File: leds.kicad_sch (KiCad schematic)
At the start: 193 parts

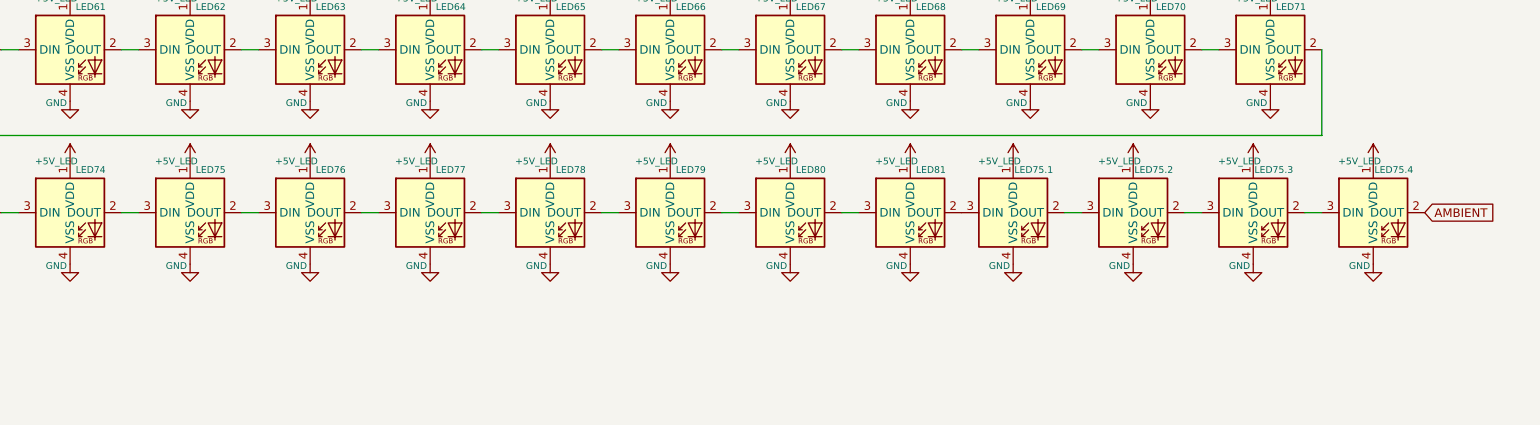
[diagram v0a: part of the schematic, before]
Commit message: Implemented multiple leds for spacebar
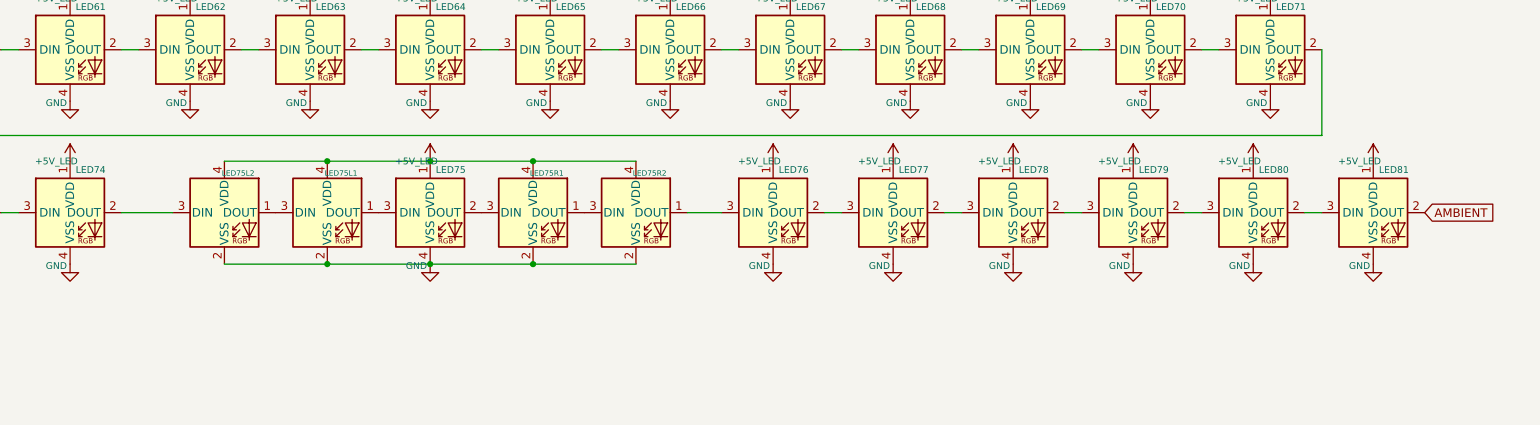
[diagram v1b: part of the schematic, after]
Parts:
- removed LED75.1, LED75.2, LED75.3, LED75.4: SK6812, PCM_marbastlib-various:LED_6028R, symbol PCM_marbastlib-various:SK6812MINI-E
- added LED75L1, LED75L2, LED75R1, LED75R2: WS2812_2020, PCM_marbastlib-various:LED_WS2812_2020, symbol PCM_marbastlib-various:WS2812_2020
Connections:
- net +5V_LED: now also LED75L1.4 (VDD), LED75L2.4 (VDD), LED75R1.4 (VDD), LED75R2.4 (VDD)
- net AMBIENT: now also LED81.2 (DOUT)
- net GND: now also LED75L1.2 (VSS), LED75L2.2 (VSS), LED75R1.2 (VSS), LED75R2.2 (VSS)
- net at LED74.2 (DOUT): now also LED75L2.3 (DIN); no longer LED75.3 (DIN)
- net at LED76.3 (DIN): now also LED75R2.1 (DOUT); no longer LED75.2 (DOUT)
- new net: LED75R1.1 (DOUT), LED75R2.3 (DIN)
- new net: LED75L1.3 (DIN), LED75L2.1 (DOUT)
- new net: LED75.2 (DOUT), LED75R1.3 (DIN)
- new net: LED75.3 (DIN), LED75L1.1 (DOUT)
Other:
- moved on the sheet: LED75, LED76, LED77, LED78, LED79, LED80, LED81

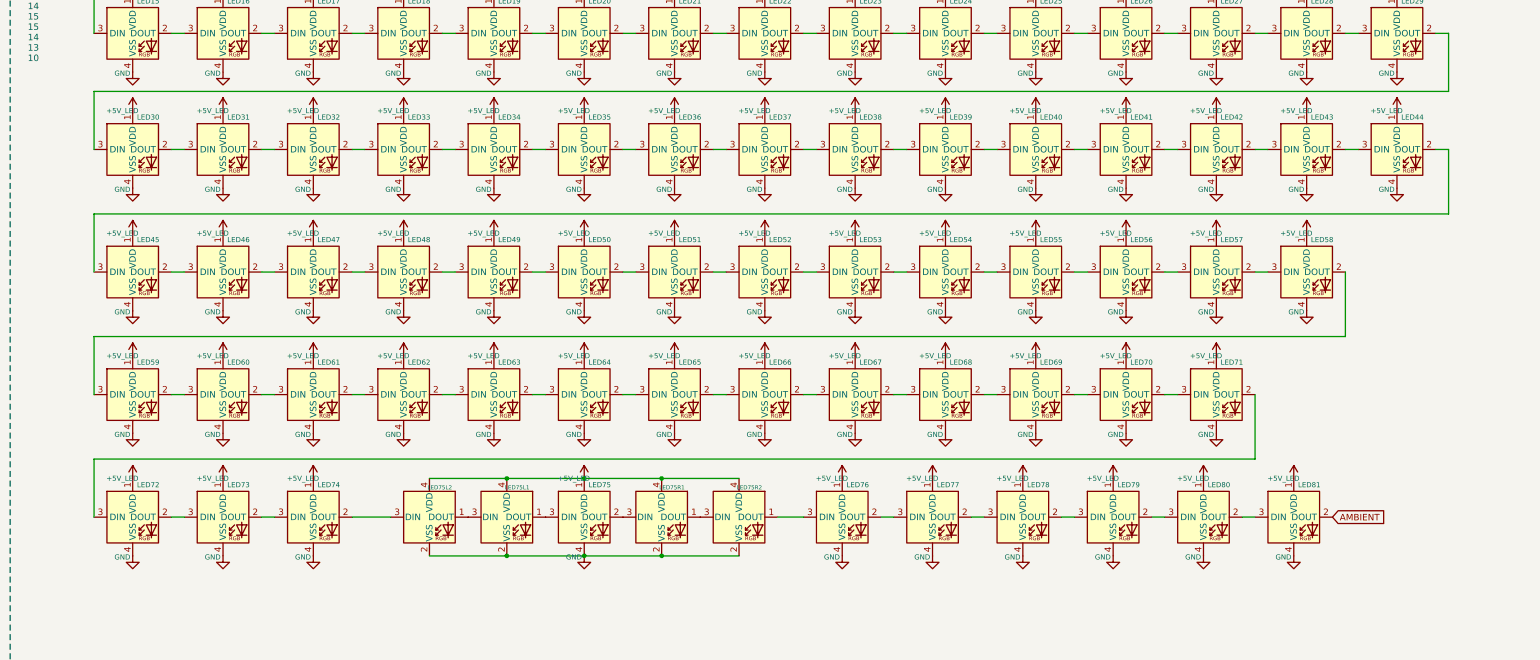
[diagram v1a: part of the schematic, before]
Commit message: Rev 2: Major PCB rework — haptic motor, MicroSD, NTC, CTP, split spacebar
- Added ERM haptic motor with BSS138 MOSFET driver on GP21
- Added MicroSD card slot (MSD-1-A, push-in/auto-eject)
- Added NTC thermistor with voltage divider
- Added 4-pin 0.5mm FPC connector for capacitive touch panel
- Added ferrite beads (0603 600R, 0805) for power filtering
- Added 1N4148WT protection diode and test point
- Split spacebar support: HE45 alternate 1.75u stabilizer footprint
- Full PCB re-route with 4-layer switch footprints
- All 81 hall sensors relabeled with key names in schematic
- Relaxed DRC (text height, via diameter), new via size 0.6/0.2
- Added CHANGELOG.md and wiring.cpp MUX mapping reference
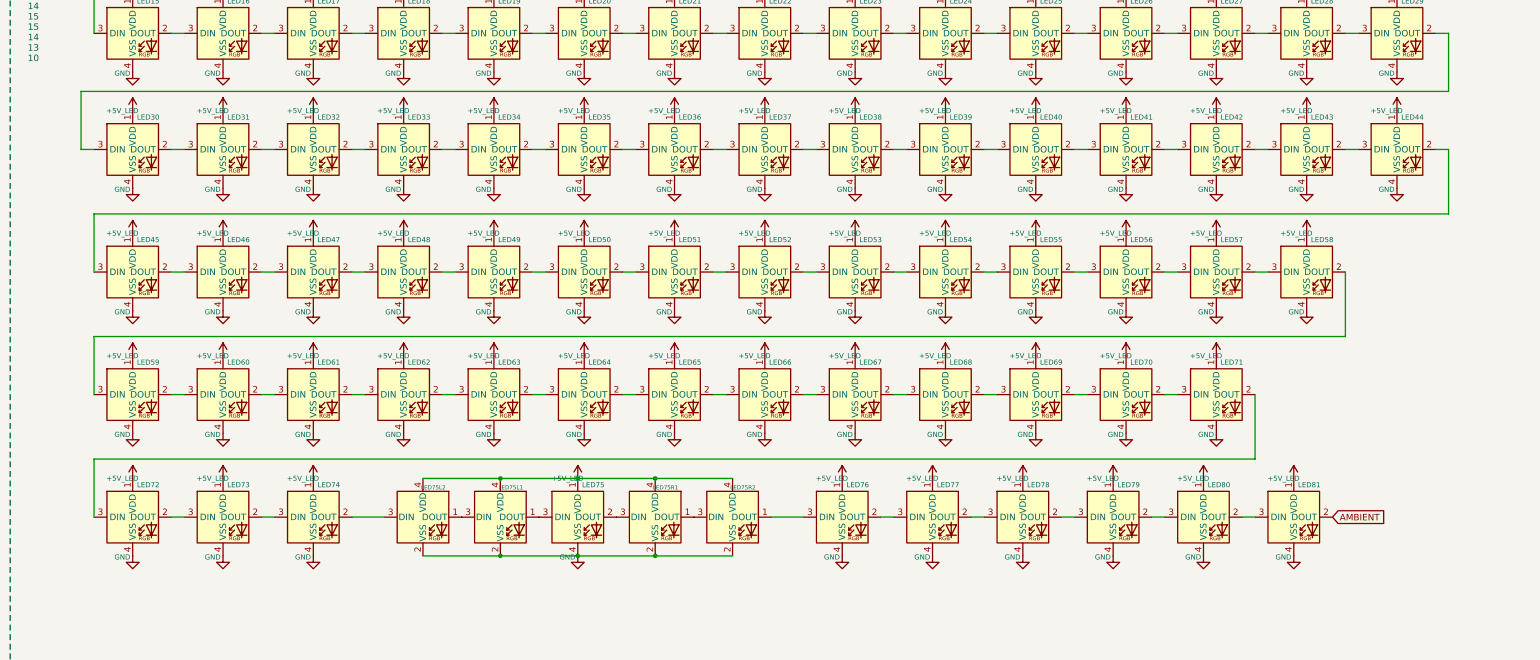
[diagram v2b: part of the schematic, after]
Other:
- moved on the sheet: LED75, LED75L1, LED75L2, LED75R1, LED75R2
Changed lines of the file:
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@@
 	)
 	(junction
-		(at 127 158.75)
+		(at 125.73 158.75)
 		(diameter 0)
 		(color 0 0 0 0)
@@
 	)
 	(junction
-		(at 111.76 158.75)
+		(at 110.49 158.75)
 		(diameter 0)
 		(color 0 0 0 0)
@@
 	)
 	(junction
-		(at 142.24 158.75)
+		(at 140.97 158.75)
 		(diameter 0)
 		(color 0 0 0 0)
@@
 	)
 	(junction
-		(at 127 173.99)
+		(at 125.73 173.99)
 		(diameter 0)
 		(color 0 0 0 0)
@@
 	)
 	(junction
-		(at 142.24 173.99)
+		(at 140.97 173.99)
 		(diameter 0)
 		(color 0 0 0 0)
@@
 	)
 	(junction
-		(at 111.76 173.99)
+		(at 110.49 173.99)
 		(diameter 0)
 		(color 0 0 0 0)
@@
 	(wire
 		(pts
-			(xy 30.48 82.55) (xy 297.18 82.55)
+			(xy 27.94 82.55) (xy 297.18 82.55)
 		)
 		(stroke
@@
 	(wire
 		(pts
-			(xy 142.24 173.99) (xy 157.48 173.99)
+			(xy 140.97 173.99) (xy 156.21 173.99)
 		)
 		(stroke
@@
 	(wire
 		(pts
-			(xy 111.76 173.99) (xy 127 173.99)
+			(xy 110.49 173.99) (xy 125.73 173.99)
 		)
 		(stroke
@@
 	(wire
 		(pts
-			(xy 81.28 166.37) (xy 88.9 166.37)
+			(xy 81.28 166.37) (xy 87.63 166.37)
 		)
 		(stroke
@@
 	(wire
 		(pts
-			(xy 165.1 166.37) (xy 170.18 166.37)
+			(xy 163.83 166.37) (xy 170.18 166.37)
 		)
 		(stroke
@@
 	(wire
 		(pts
+			(xy 27.94 93.98) (xy 30.48 93.98)
+		)
+		(stroke
+			(width 0)
+			(type default)
+		)
+	)
+	(wire
+		(pts
 			(xy 297.18 58.42) (xy 30.48 58.42)
 		)
@@
 	(wire
 		(pts
-			(xy 30.48 93.98) (xy 30.48 82.55)
+			(xy 27.94 93.98) (xy 27.94 82.55)
 		)
 		(stroke
@@
 	(wire
 		(pts
-			(xy 142.24 158.75) (xy 157.48 158.75)
+			(xy 140.97 158.75) (xy 156.21 158.75)
 		)
 		(stroke
@@
 	(wire
 		(pts
-			(xy 127 158.75) (xy 142.24 158.75)
+			(xy 125.73 158.75) (xy 140.97 158.75)
 		)
 		(stroke
@@
 	(wire
 		(pts
-			(xy 127 173.99) (xy 142.24 173.99)
+			(xy 125.73 173.99) (xy 140.97 173.99)
 		)
 		(stroke
@@
 	(wire
 		(pts
-			(xy 111.76 158.75) (xy 127 158.75)
+			(xy 110.49 158.75) (xy 125.73 158.75)
 		)
 		(stroke
@@
 	(wire
 		(pts
-			(xy 96.52 158.75) (xy 111.76 158.75)
+			(xy 95.25 158.75) (xy 110.49 158.75)
 		)
 		(stroke
@@
 	(wire
 		(pts
-			(xy 96.52 173.99) (xy 111.76 173.99)
+			(xy 95.25 173.99) (xy 110.49 173.99)
 		)
 		(stroke
@@
 	(symbol
 		(lib_id "power:+5V")
-		(at 127 158.75 0)
+		(at 125.73 158.75 0)
 		(unit 1)
 		(exclude_from_sim no)
@@
 		(dnp no)
 		(property "Reference" "#PWR0213"
-			(at 127 162.56 0)
+			(at 125.73 162.56 0)
 			(effects
 				(font
@@
 		)
 		(property "Value" "+5V_LED"
-			(at 124.968 158.75 0)
+			(at 123.698 158.75 0)
 			(effects
 				(font
@@
 		)
 		(property "Footprint" ""
-			(at 127 158.75 0)
+			(at 125.73 158.75 0)
 			(effects
 				(font
@@
 		)
 		(property "Datasheet" ""
-			(at 127 158.75 0)
+			(at 125.73 158.75 0)
 			(effects
 				(font
@@
 		)
 		(property "Description" "Power symbol creates a global label with name \"+5V\""
-			(at 127 158.75 0)
+			(at 125.73 158.75 0)
 			(effects
 				(font
@@
 	(symbol
 		(lib_id "PCM_marbastlib-various:WS2812_2020")
-		(at 157.48 166.37 0)
+		(at 156.21 166.37 0)
 		(unit 1)
 		(exclude_from_sim no)
@@
 		(dnp no)
 		(property "Reference" "LED75R2"
-			(at 159.512 160.528 0)
+			(at 158.242 160.528 0)
 			(effects
 				(font
@@
 		)
 		(property "Value" "WS2812_2020"
-			(at 170.18 162.4898 0)
+			(at 168.91 162.4898 0)
 			(effects
 				(font
@@
 		)
 		(property "Footprint" "PCM_marbastlib-various:LED_WS2812_2020"
-			(at 158.75 173.99 0)
+			(at 157.48 173.99 0)
 			(effects
 				(font
@@
 		)
 		(property "Datasheet" "https://www.world-semi.com/DownLoadFile/139"
-			(at 160.02 175.895 0)
+			(at 158.75 175.895 0)
 			(effects
 				(font
@@
 		)
 		(property "Description" "2020 SMD adressable RGB LED with integrated controller"
-			(at 157.48 166.37 0)
+			(at 156.21 166.37 0)
 			(effects
 				(font
@@
 	(symbol
 		(lib_id "PCM_marbastlib-various:WS2812_2020")
-		(at 96.52 166.37 0)
+		(at 95.25 166.37 0)
 		(unit 1)
 		(exclude_from_sim no)
@@
 		(dnp no)
 		(property "Reference" "LED75L2"
-			(at 98.552 160.528 0)
+			(at 97.282 160.528 0)
 			(effects
 				(font
@@
 		)
 		(property "Value" "WS2812_2020"
-			(at 109.22 162.4898 0)
+			(at 107.95 162.4898 0)
 			(effects
 				(font
@@
 		)
 		(property "Footprint" "PCM_marbastlib-various:LED_WS2812_2020"
-			(at 97.79 173.99 0)
+			(at 96.52 173.99 0)
 			(effects
 				(font
@@
 		)
 		(property "Datasheet" "https://www.world-semi.com/DownLoadFile/139"
-			(at 99.06 175.895 0)
+			(at 97.79 175.895 0)
 			(effects
 				(font
@@
 		)
 		(property "Description" "2020 SMD adressable RGB LED with integrated controller"
-			(at 96.52 166.37 0)
+			(at 95.25 166.37 0)
 			(effects
 				(font
@@
 	(symbol
 		(lib_id "power:GND")
-		(at 127 173.99 0)
+		(at 125.73 173.99 0)
 		(unit 1)
 		(exclude_from_sim no)
@@
 		(dnp no)
 		(property "Reference" "#PWR0225"
-			(at 127 180.34 0)
+			(at 125.73 180.34 0)
 			(effects
 				(font
@@
 		)
 		(property "Value" "GND"
-			(at 124.968 174.244 0)
+			(at 123.698 174.244 0)
 			(effects
 				(font
@@
 		)
 		(property "Footprint" ""
-			(at 127 173.99 0)
+			(at 125.73 173.99 0)
 			(effects
 				(font
@@
 		)
 		(property "Datasheet" ""
-			(at 127 173.99 0)
+			(at 125.73 173.99 0)
 			(effects
 				(font
@@
 		)
 		(property "Description" "Power symbol creates a global label with name \"GND\" , ground"
-			(at 127 173.99 0)
+			(at 125.73 173.99 0)
 			(effects
 				(font
@@
 	(symbol
 		(lib_id "PCM_marbastlib-various:SK6812MINI-E")
-		(at 127 166.37 0)
+		(at 125.73 166.37 0)
 		(unit 1)
 		(exclude_from_sim no)
@@
 		(dnp no)
 		(property "Reference" "LED75"
-			(at 130.048 160.02 0)
+			(at 128.778 160.02 0)
 			(effects
 				(font
@@
 		)
 		(property "Value" "SK6812"
-			(at 137.16 162.4898 0)
+			(at 135.89 162.4898 0)
 			(effects
 				(font
@@
 		)
 		(property "Footprint" "PCM_marbastlib-various:LED_6028R"
-			(at 127 166.37 0)
+			(at 125.73 166.37 0)
 			(effects
 				(font
@@
 		)
 		(property "Datasheet" ""
-			(at 127 166.37 0)
+			(at 125.73 166.37 0)
 			(effects
 				(font
@@
 		)
 		(property "Description" "Reverse mount adressable LED (WS2812 protocol)"
-			(at 127 166.37 0)
+			(at 125.73 166.37 0)
 			(effects
 				(font
@@
 		)
 		(property "LCSC" "C5149201 "
-			(at 127 166.37 0)
+			(at 125.73 166.37 0)
 			(effects
 				(font
@@
 	(symbol
 		(lib_id "PCM_marbastlib-various:WS2812_2020")
-		(at 111.76 166.37 0)
+		(at 110.49 166.37 0)
 		(unit 1)
 		(exclude_from_sim no)
@@
 		(dnp no)
 		(property "Reference" "LED75L1"
-			(at 113.792 160.528 0)
+			(at 112.522 160.528 0)
 			(effects
 				(font
@@
 		)
 		(property "Value" "WS2812_2020"
-			(at 124.46 162.4898 0)
+			(at 123.19 162.4898 0)
 			(effects
 				(font
@@
 		)
 		(property "Footprint" "PCM_marbastlib-various:LED_WS2812_2020"
-			(at 113.03 173.99 0)
+			(at 111.76 173.99 0)
 			(effects
 				(font
@@
 		)
 		(property "Datasheet" "https://www.world-semi.com/DownLoadFile/139"
-			(at 114.3 175.895 0)
+			(at 113.03 175.895 0)
 			(effects
 				(font
@@
 		)
 		(property "Description" "2020 SMD adressable RGB LED with integrated controller"
-			(at 111.76 166.37 0)
+			(at 110.49 166.37 0)
 			(effects
 				(font
@@
 	(symbol
 		(lib_id "PCM_marbastlib-various:WS2812_2020")
-		(at 142.24 166.37 0)
+		(at 140.97 166.37 0)
 		(unit 1)
 		(exclude_from_sim no)
@@
 		(dnp no)
 		(property "Reference" "LED75R1"
-			(at 144.272 160.528 0)
+			(at 143.002 160.528 0)
 			(effects
 				(font
@@
 		)
 		(property "Value" "WS2812_2020"
-			(at 154.94 162.4898 0)
+			(at 153.67 162.4898 0)
 			(effects
 				(font
@@
 		)
 		(property "Footprint" "PCM_marbastlib-various:LED_WS2812_2020"
-			(at 143.51 173.99 0)
+			(at 142.24 173.99 0)
 			(effects
 				(font
@@
 		)
 		(property "Datasheet" "https://www.world-semi.com/DownLoadFile/139"
-			(at 144.78 175.895 0)
+			(at 143.51 175.895 0)
 			(effects
 				(font
@@
 		)
 		(property "Description" "2020 SMD adressable RGB LED with integrated controller"
-			(at 142.24 166.37 0)
+			(at 140.97 166.37 0)
 			(effects
 				(font

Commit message: VLT PCB rev: dual TFT connector, RKJXT1F42001 footprint, LED expansion header
- Add 12-pin TFT connector alongside existing 8-pin for CTP-integrated display option
- Superimpose RKJXT1F42001 5-way joystick footprint on EC11 encoder for testing
- Add LED expansion header for additional RGB zones
- Update production files
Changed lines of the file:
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@@
-		)
-	)
-	(label "LED_EXP"
-		(at 317.5 231.14 0)
-		(effects
-			(font
-				(size 1.27 1.27)
-			)
-			(justify left bottom)
 		)
 	)
@@
 			(effects
 				(font
+					(size 1.27 1.27)
+				)
+				(justify left)
+				(hide yes)
+			)
+		)
+	)
+	(global_label "LED_EXP"
+		(shape input)
+		(at 317.5 231.14 0)
+		(fields_autoplaced yes)
+		(effects
+			(font
+				(size 1.27 1.27)
+			)
+			(justify left)
+		)
+		(property "Intersheetrefs" "${INTERSHEET_REFS}"
+			(at 328.5284 231.14 0)
+			(effects
+				(font
